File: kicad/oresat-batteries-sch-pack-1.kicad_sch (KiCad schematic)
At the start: 79 parts, among them Q12 Q-VISHAY-MOSFET-PCH-POWERPAK-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, Q13 Q-VISHAY-MOSFET-PCH-POWERPAK-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, Q14 NTR4101, Q15 NTR4101, Q16 Q-VISHAY-MOSFET-PCH-POWERPAK-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, Q17 Q-VISHAY-MOSFET-PCH-POWERPAK-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, Q18 Q-VISHAY-MOSFET-PCH-POWERPAK-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, Q19 Q-VISHAY-MOSFET-PCH-POWERPAK-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, Q6 PM45VEN, Q7 PM45VEN, Q8 PM45VEN, Q9 PM45VEN, U10 LTC4412, U11 LTC4412, U12 MAX17205G, U8 S-8209AXXT, U9 S-8209AXXT

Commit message: Updating KiCAD import of EAGLE battery card v3.0 and calling it v3.1 because the gerber files will definitely be different and we'll probably implement a few small changes. Reimports, renames, and fixes .gitignore file. Oh and makes the worksheets pretty.
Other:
- note removed: "1.0"
- note removed: "OreSat battery Card - Battery Pack 1"
- title: (none) -> OreSat Battery Card - Pack 1 (Bottom)
- moved on the sheet: B1, B2, C15, C16, C17, C18, C19, C20, C21, C22, C23, C24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

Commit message: Kicad import try #3. Now with DXFs from custom EAGLE layers. Schematic worksheets and names updated.
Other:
- title: OreSat Battery Card - Pack 1 (Bottom) -> OreSat Battery Card

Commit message: Move main connector to kicad libraries; start updating text size.
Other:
- title: OreSat Battery Card -> OreSat Battery Card - Pack 1 (Bottom)
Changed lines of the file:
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@@
   (paper "B")
   (title_block
-    (title "OreSat Battery Card")
+    (title "OreSat Battery Card - Pack 1 (Bottom)")
     (date "2023-12-02")
     (rev "3.1")

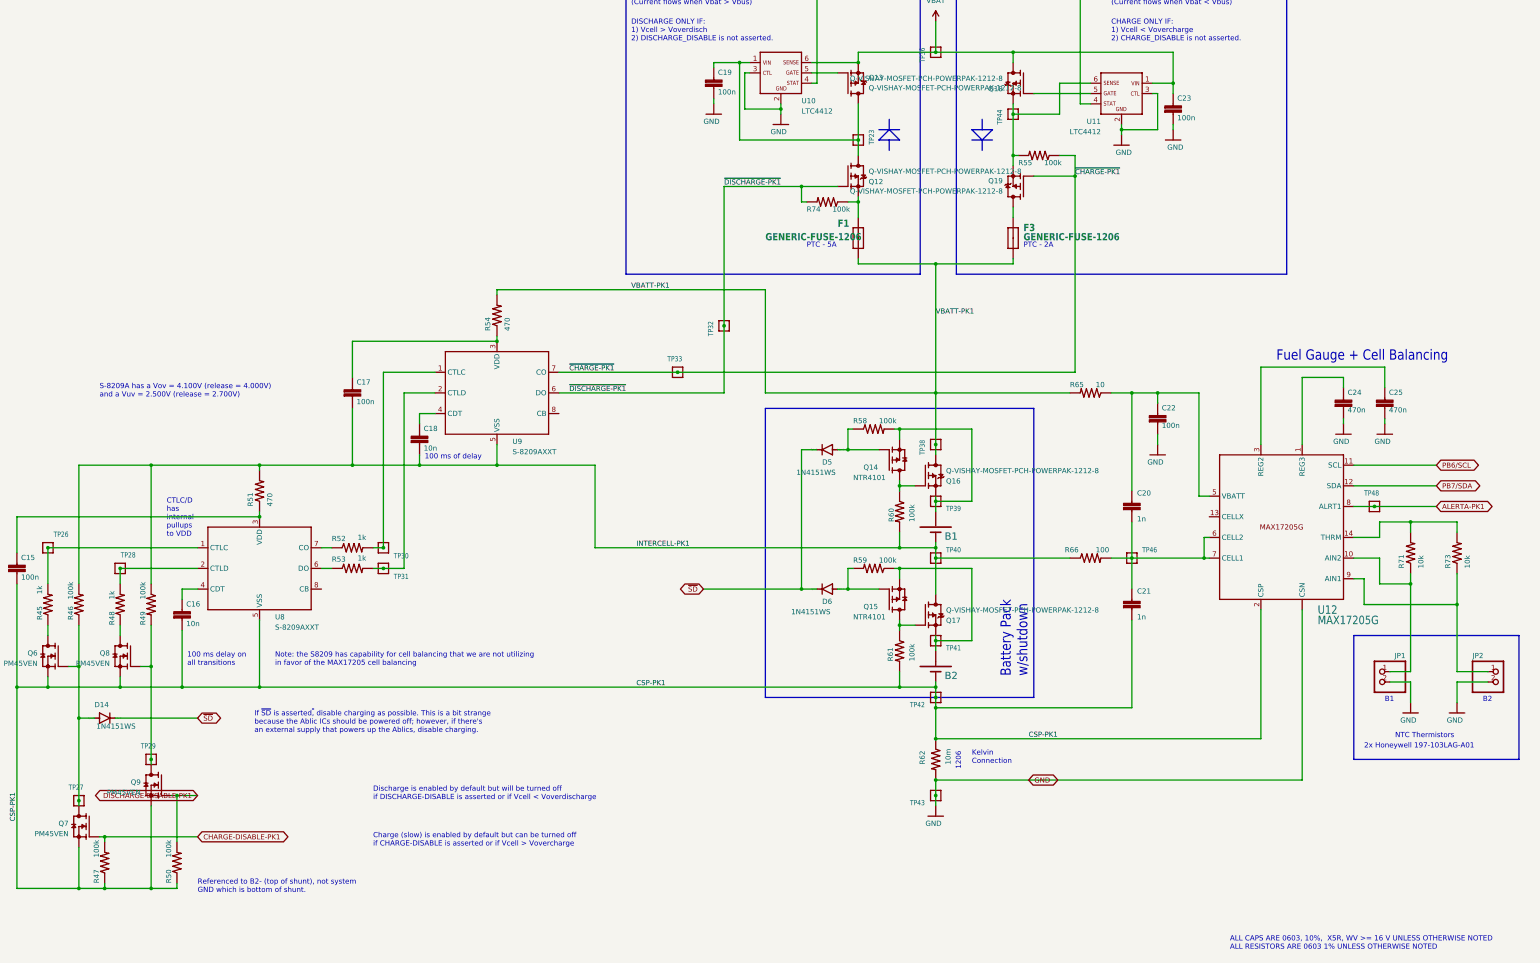
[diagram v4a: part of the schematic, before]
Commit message: Updated ground planes, battery foot prints, zones needs more work.
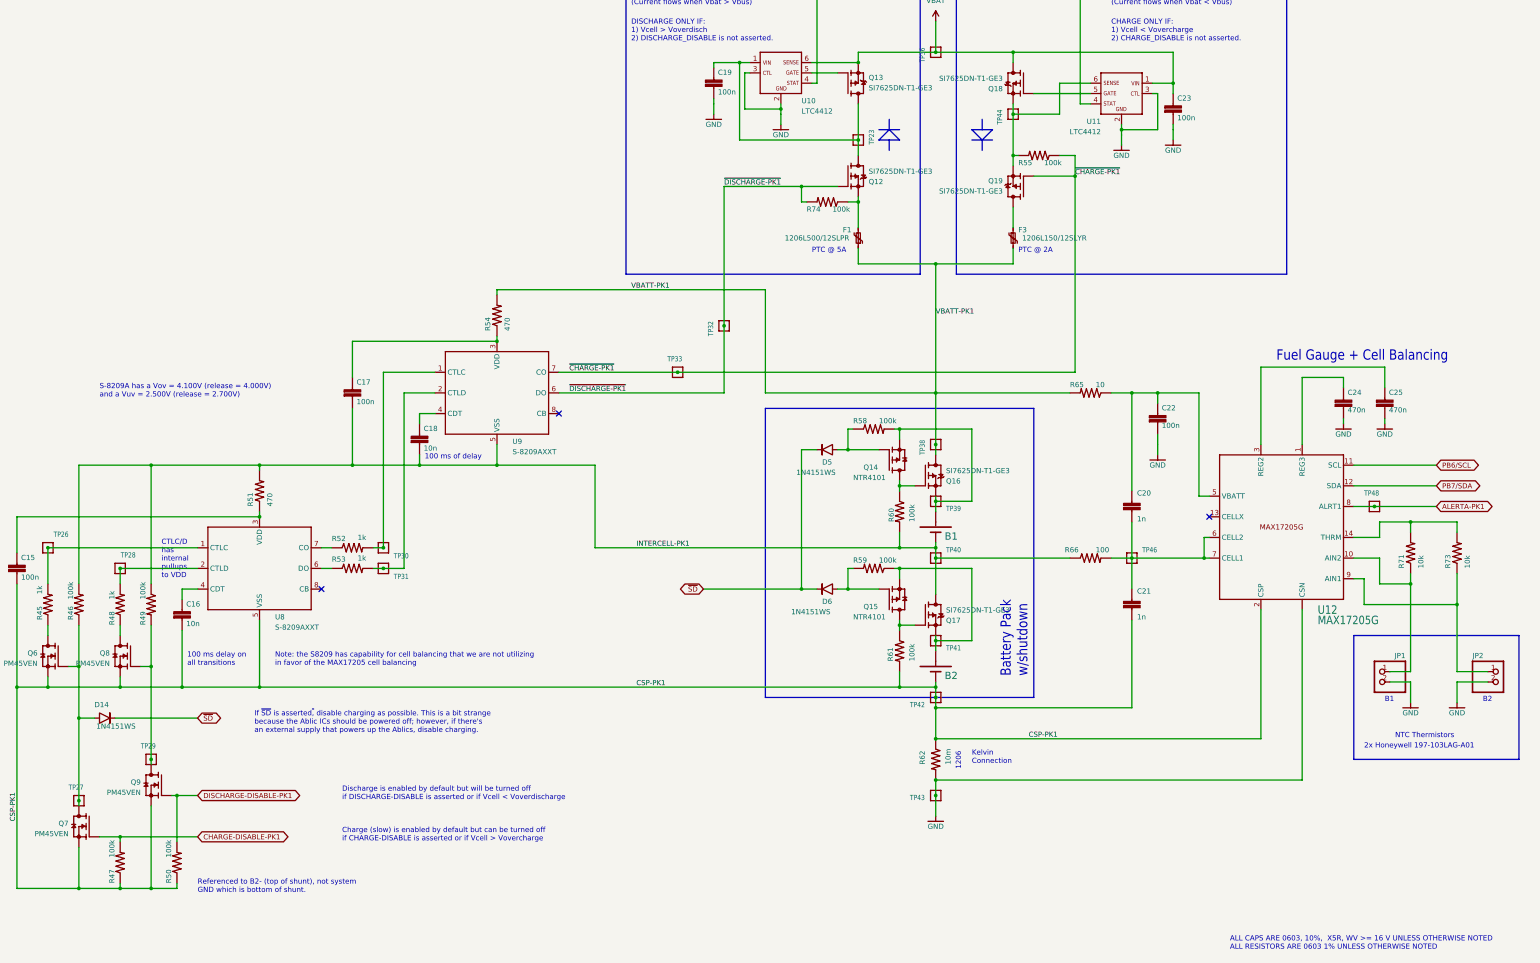
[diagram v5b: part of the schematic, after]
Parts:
- D14, D5, D6: footprint oresat-batteries:SOD323-R -> Diode_SMD:D_SOD-323; symbol oresat-batteries-eagle-import:DIODE-SOD323-R -> oresat-diodes:1N4151WS-HE3; DIS Digi-Key -> (none); DPN 112-1N4151WS-E3-08CT-ND -> (none); MFR Vishay -> (none); MPN 1N4151WS-E3-08 -> (none)
- F1: value GENERIC-FUSE-1206 -> 1206L500/12SLPR; footprint oresat-batteries:1206-C -> oresat-passives:1206-C; symbol oresat-batteries-eagle-import:GENERIC-FUSE-1206 -> Device:Polyfuse_Small; DIS Digi-Key -> (none); DPN F9966CT-ND -> (none); MFR LittleFuse -> (none); MPN NANOSMD350LR-C-2 -> (none)
- F3: value GENERIC-FUSE-1206 -> 1206L150/12SLYR; footprint oresat-batteries:1206-C -> oresat-passives:1206-C; symbol oresat-batteries-eagle-import:GENERIC-FUSE-1206 -> Device:Polyfuse_Small; DIS Digi-Key -> (none); DPN F9966CT-ND -> (none); MFR LittleFuse -> (none); MPN NANOSMD350LR-C-2 -> (none)
- Q12, Q13, Q16, Q17, Q18, Q19: value Q-VISHAY-MOSFET-PCH-POWERPAK-1212-8 -> SI7625DN-T1-GE3
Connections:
- net CSP-PK1: now also B2.2 (NEG); no longer B2.NEG-T (NEG)
- net INTERCELL-PK1: now also B1.2 (NEG); no longer B1.NEG-T (NEG)
- net VBATT-PK1: now also F1.1; no longer F1.2 (P$2)
- net ~{SD}: now also D14.1, D5.1, D6.1; no longer D14.C, D5.C, D6.C
- net at Q6.1 (G), Q7.3 (D), R46.1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: now also D14.2; no longer D14.A
- net at Q15.2 (S), Q17.1 (S), Q17.2 (S)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: now also B2.1 (POS); no longer B2.POS-T (POS)
- net at Q15.1 (G), R59.2: now also D6.2; no longer D6.A
- net at Q14.2 (S), Q16.1 (S), Q16.2 (S)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: now also B1.1 (POS); no longer B1.POS-T (POS)
- net at Q14.1 (G), R58.1: now also D5.2; no longer D5.A
- net at Q12.1 (S), Q12.2 (S), Q12.3 (S)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: now also F1.2; no longer F1.1 (P$1)
- no-connect marks 0 -> 3
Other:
- note added: "PTC @ 2A"
- note added: "PTC @ 5A"
- note removed: "PTC - 2A"
- note removed: "PTC - 5A"
- moved on the sheet: R47

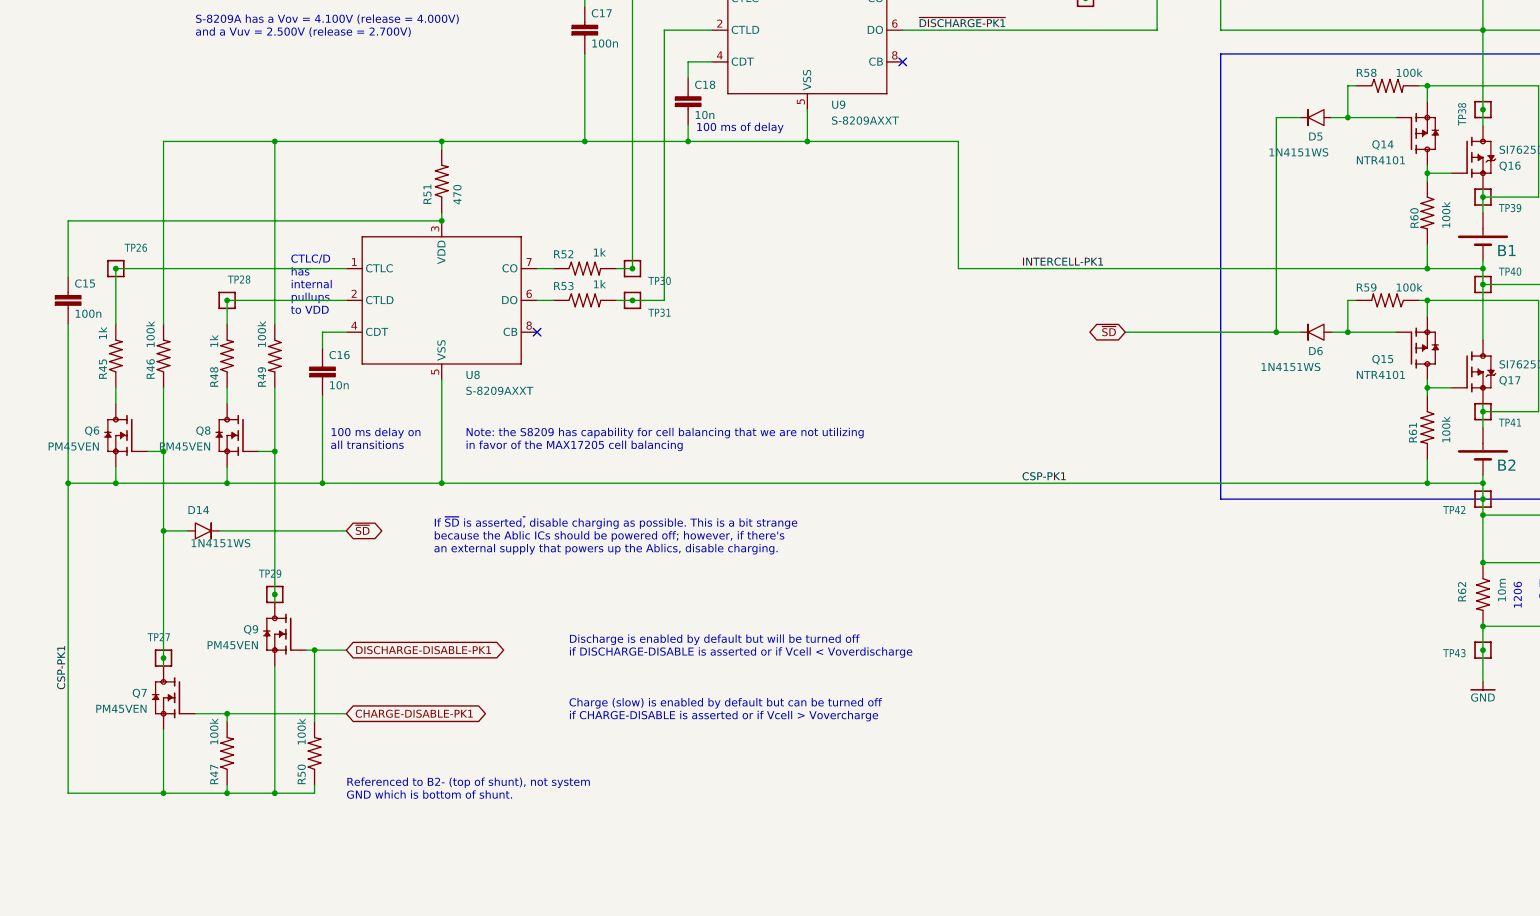
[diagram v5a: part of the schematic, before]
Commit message: better schematic layout (no netlist changes) on battery packs, and updated DRUs and fixed some minor DRU issues.
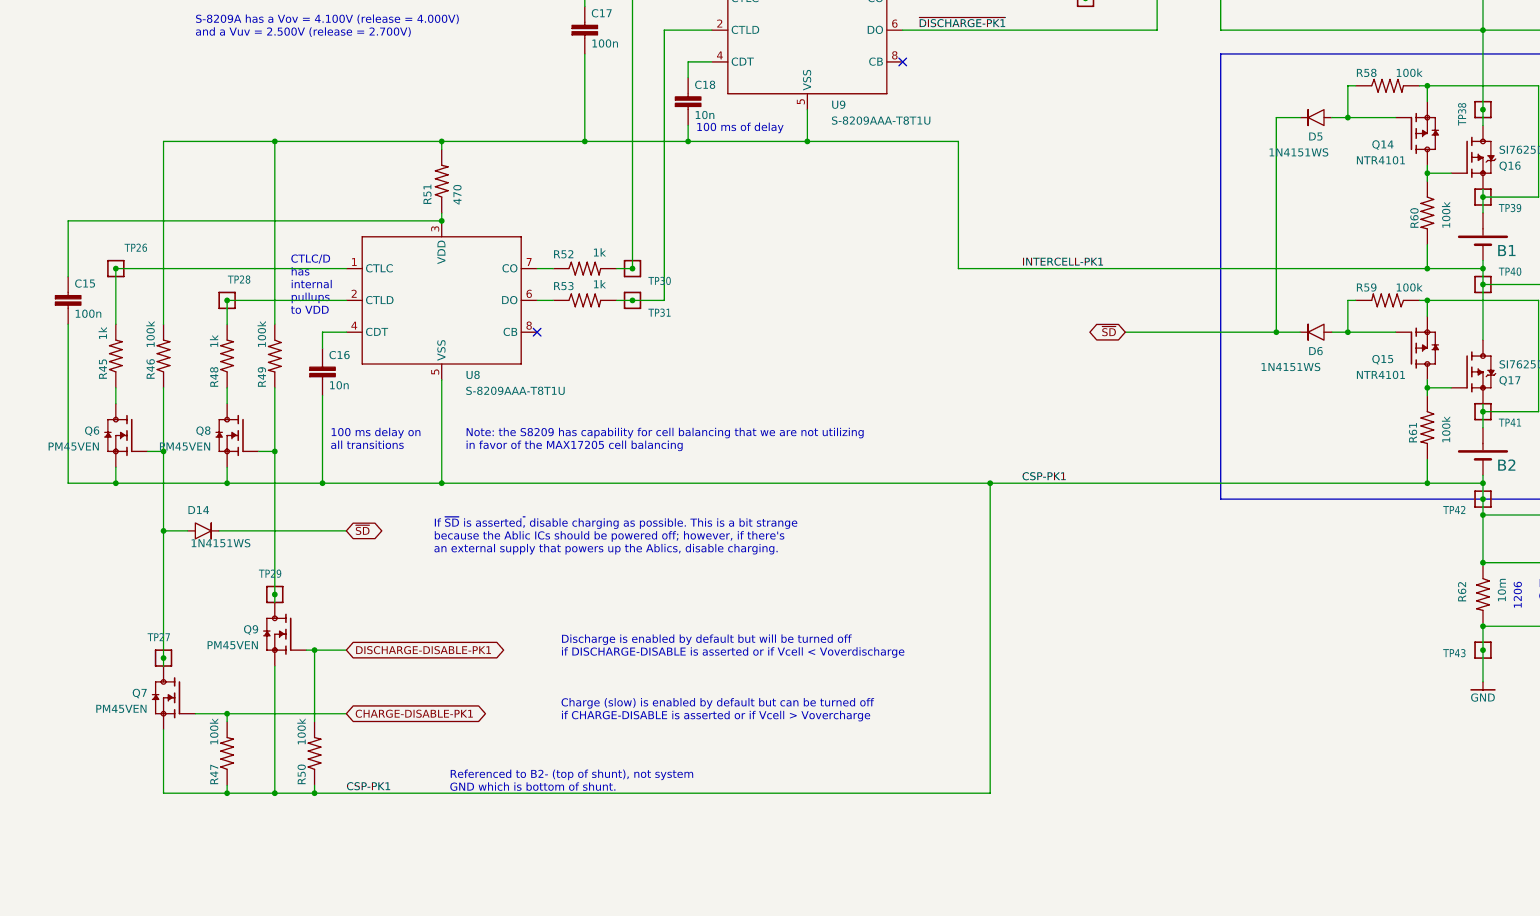
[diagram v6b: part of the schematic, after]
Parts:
- U8, U9: value S-8209AXXT -> S-8209AAA-T8T1U
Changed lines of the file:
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@@
   (junction (at 195.58 123.19) (diameter 0) (color 0 0 0 0)
   )
+  (junction (at 72.39 250.19) (diameter 0) (color 0 0 0 0)
+  )
   (junction (at 250.19 171.45) (diameter 0) (color 0 0 0 0)
   )
+  (junction (at 180.34 200.66) (diameter 0) (color 0 0 0 0)
+  )
   (junction (at 375.92 160.02) (diameter 0) (color 0 0 0 0)
   )
@@
   (junction (at 73.66 200.66) (diameter 0) (color 0 0 0 0)
   )
-  (junction (at 33.02 200.66) (diameter 0) (color 0 0 0 0)
-  )
   (junction (at 229.87 17.78) (diameter 0) (color 0 0 0 0)
   )
@@
   (junction (at 307.34 128.27) (diameter 0) (color 0 0 0 0)
   )
-  (junction (at 48.26 250.19) (diameter 0) (color 0 0 0 0)
-  )
   (junction (at 92.71 200.66) (diameter 0) (color 0 0 0 0)
   )
@@
     (stroke (width 0.508) (type solid))
   )
+  (wire (pts (xy 72.39 250.19) (xy 180.34 250.19))
+    (stroke (width 0.1524) (type solid))
+  )
   (polyline (pts (xy 270.51 63.5) (xy 270.51 60.96))
     (stroke (width 0.1524) (type solid))
@@
     (stroke (width 0.508) (type solid))
   )
-  (wire (pts (xy 33.02 250.19) (xy 48.26 250.19))
-    (stroke (width 0.1524) (type solid))
-  )
   (polyline (pts (xy 247.65 63.5) (xy 245.11 63.5))
     (stroke (width 0.1524) (type solid))
@@
     (stroke (width 0.508) (type solid))
   )
-  (wire (pts (xy 250.19 200.66) (xy 92.71 200.66))
+  (wire (pts (xy 250.19 200.66) (xy 180.34 200.66))
     (stroke (width 0.1524) (type solid))
   )
@@
     (stroke (width 0.508) (type solid))
   )
+  (wire (pts (xy 180.34 200.66) (xy 92.71 200.66))
+    (stroke (width 0.1524) (type solid))
+  )
   (wire (pts (xy 33.02 200.66) (xy 40.64 200.66))
     (stroke (width 0.1524) (type solid))
@@
     (stroke (width 0.1524) (type solid))
   )
-  (wire (pts (xy 33.02 200.66) (xy 33.02 250.19))
-    (stroke (width 0.1524) (type solid))
-  )
   (wire (pts (xy 375.92 162.56) (xy 375.92 160.02))
     (stroke (width 0.1524) (type solid))
@@
     (stroke (width 0.1524) (type solid))
   )
+  (wire (pts (xy 180.34 250.19) (xy 180.34 200.66))
+    (stroke (width 0.1524) (type solid))
+  )
   (wire (pts (xy 213.36 46.99) (xy 210.82 46.99))
     (stroke (width 0.1524) (type solid))
@@
   )
   (text "Discharge is enabled by default but will be turned off\nif DISCHARGE-DISABLE is asserted or if Vcell < Voverdischarge"
-    (at 113.03 228.6 0)
+    (at 111.76 228.6 0)
     (effects (font (size 1.27 1.27)) (justify left bottom))
   )
@@
   )
   (text "Charge (slow) is enabled by default but can be turned off\nif CHARGE-DISABLE is asserted or if Vcell > Vovercharge"
-    (at 113.03 238.76 0)
+    (at 111.76 238.76 0)
     (effects (font (size 1.27 1.27)) (justify left bottom))
   )
@@
   )
   (text "Referenced to B2- (top of shunt), not system\nGND which is bottom of shunt."
-    (at 77.47 251.46 0)
+    (at 93.98 250.19 0)
     (effects (font (size 1.27 1.27)) (justify left bottom))
   )
@@
     (effects (font (size 1.2446 1.2446)) (justify left bottom))
   )
-  (label "CSP-PK1" (at 33.02 233.68 90) (fields_autoplaced)
+  (label "CSP-PK1" (at 77.47 250.19 0) (fields_autoplaced)
     (effects (font (size 1.2446 1.2446)) (justify left bottom))
   )
@@
       (effects (font (size 1.27 1.27)) hide)
     )
-    (property "Datasheet" "" (at 220.98 49.53 0)
+    (property "Datasheet" "https://www.analog.com/media/en/technical-documentation/data-sheets/4412hvfs.pdf" (at 220.98 49.53 0)
       (effects (font (size 1.27 1.27)) hide)
     )
@@
       (effects (font (size 1.27 1.27)) (justify left bottom))
     )
-    (property "Value" "S-8209AXXT" (at 96.52 186.69 0)
+    (property "Value" "S-8209AAA-T8T1U" (at 96.52 186.69 0)
       (effects (font (size 1.27 1.27)) (justify left bottom))
     )
@@
       (effects (font (size 1.27 1.27)) hide)
     )
-    (property "Datasheet" "" (at 92.71 171.45 0)
+    (property "Datasheet" "https://www.ablic.com/en/doc/datasheet/battery_protection/S8209A_E.pdf" (at 92.71 171.45 0)
       (effects (font (size 1.27 1.27)) hide)
     )
@@
       (effects (font (size 1.27 1.27)) hide)
     )
-    (property "Datasheet" "" (at 304.8 54.61 0)
+    (property "Datasheet" "https://www.analog.com/media/en/technical-documentation/data-sheets/4412hvfs.pdf" (at 304.8 54.61 0)
       (effects (font (size 1.27 1.27)) hide)
     )
@@
       (effects (font (size 1.27 1.27)) (justify left bottom))
     )
-    (property "Value" "S-8209AXXT" (at 154.94 143.51 0)
+    (property "Value" "S-8209AAA-T8T1U" (at 154.94 143.51 0)
       (effects (font (size 1.27 1.27)) (justify left bottom))
     )
@@
       (effects (font (size 1.27 1.27)) hide)
     )
-    (property "Datasheet" "" (at 151.13 128.27 0)
+    (property "Datasheet" "https://www.ablic.com/en/doc/datasheet/battery_protection/S8209A_E.pdf" (at 151.13 128.27 0)
       (effects (font (size 1.27 1.27)) hide)
     )
